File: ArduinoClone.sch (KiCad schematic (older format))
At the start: 13 parts, among them U1 DS1337S+, U2 24LC1025, U3 24LC1025, U4 ATMEGA328-AU, Y1 Crystal 32MHz, Y2 Crystal 16MHz

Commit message: added power flag
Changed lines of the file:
@@
 	7650 4850 7550 4850
 $Comp
-L power:GNDPWR #PWR?
+L power:GNDPWR #PWR0101
 U 1 1 5E9DFB73
 P 8750 5750
-F 0 "#PWR?" H 8750 5550 50  0001 C CNN
+F 0 "#PWR0101" H 8750 5550 50  0001 C CNN
 F 1 "GNDPWR" H 8754 5596 50  0000 C CNN
 F 2 "" H 8750 5700 50  0001 C CNN
@@
 	2900 1200 2900 1400
 $Comp
-L power:GNDPWR #PWR?
+L power:GNDPWR #PWR0102
 U 1 1 5E9F2D0F
 P 2900 2600
-F 0 "#PWR?" H 2900 2400 50  0001 C CNN
+F 0 "#PWR0102" H 2900 2400 50  0001 C CNN
 F 1 "GNDPWR" H 2904 2446 50  0000 C CNN
 F 2 "" H 2900 2550 50  0001 C CNN
@@
 	2600 3800 3450 3800
 $Comp
-L power:GNDPWR #PWR?
+L power:GNDPWR #PWR0103
 U 1 1 5E9FB7AB
 P 2800 4650
-F 0 "#PWR?" H 2800 4450 50  0001 C CNN
+F 0 "#PWR0103" H 2800 4450 50  0001 C CNN
 F 1 "GNDPWR" H 2804 4496 50  0000 C CNN
 F 2 "" H 2800 4600 50  0001 C CNN
@@
 ADDS2
 $Comp
-L power:GNDPWR #PWR?
+L power:GNDPWR #PWR0104
 U 1 1 5EA036F4
 P 9650 3200
-F 0 "#PWR?" H 9650 3000 50  0001 C CNN
+F 0 "#PWR0104" H 9650 3000 50  0001 C CNN
 F 1 "GNDPWR" H 9654 3046 50  0000 C CNN
 F 2 "" H 9650 3150 50  0001 C CNN
@@
 	9650 2000 9650 1700
 Wire Wire Line
-	9650 1700 7650 1700
+	9650 1700 8600 1700
 Connection ~ 7650 1700
 Wire Wire Line
@@
 	6350 2400 6200 2400
 $Comp
-L power:GNDPWR #PWR?
+L power:GNDPWR #PWR0105
 U 1 1 5EA0FFB6
 P 4750 2550
-F 0 "#PWR?" H 4750 2350 50  0001 C CNN
+F 0 "#PWR0105" H 4750 2350 50  0001 C CNN
 F 1 "GNDPWR" H 4754 2396 50  0000 C CNN
 F 2 "" H 4750 2500 50  0001 C CNN
@@
 	6150 3250 6950 3250
 $Comp
-L power:GNDPWR #PWR?
+L power:GNDPWR #PWR0106
 U 1 1 5EA19705
 P 5500 3900
-F 0 "#PWR?" H 5500 3700 50  0001 C CNN
+F 0 "#PWR0106" H 5500 3700 50  0001 C CNN
 F 1 "GNDPWR" H 5504 3746 50  0000 C CNN
 F 2 "" H 5500 3850 50  0001 C CNN
@@
 	6550 4700 6150 4700
 $Comp
-L power:GNDPWR #PWR?
+L power:GNDPWR #PWR0107
 U 1 1 5EA221DB
 P 7550 5300
-F 0 "#PWR?" H 7550 5100 50  0001 C CNN
+F 0 "#PWR0107" H 7550 5100 50  0001 C CNN
 F 1 "GNDPWR" H 7554 5146 50  0000 C CNN
 F 2 "" H 7550 5250 50  0001 C CNN
@@
 NoConn ~ 6950 4450
 NoConn ~ 6950 4550
+$Comp
+L power:PWR_FLAG #FLG0101
+U 1 1 5EA4EF3A
+P 8600 1700
+F 0 "#FLG0101" H 8600 1775 50  0001 C CNN
+F 1 "PWR_FLAG" H 8600 1873 50  0000 C CNN
+F 2 "" H 8600 1700 50  0001 C CNN
+F 3 "~" H 8600 1700 50  0001 C CNN
+	1    8600 1700
+	1    0    0    -1
+$EndComp
+Connection ~ 8600 1700
+Wire Wire Line
+	8600 1700 7650 1700
 $EndSCHEMATC

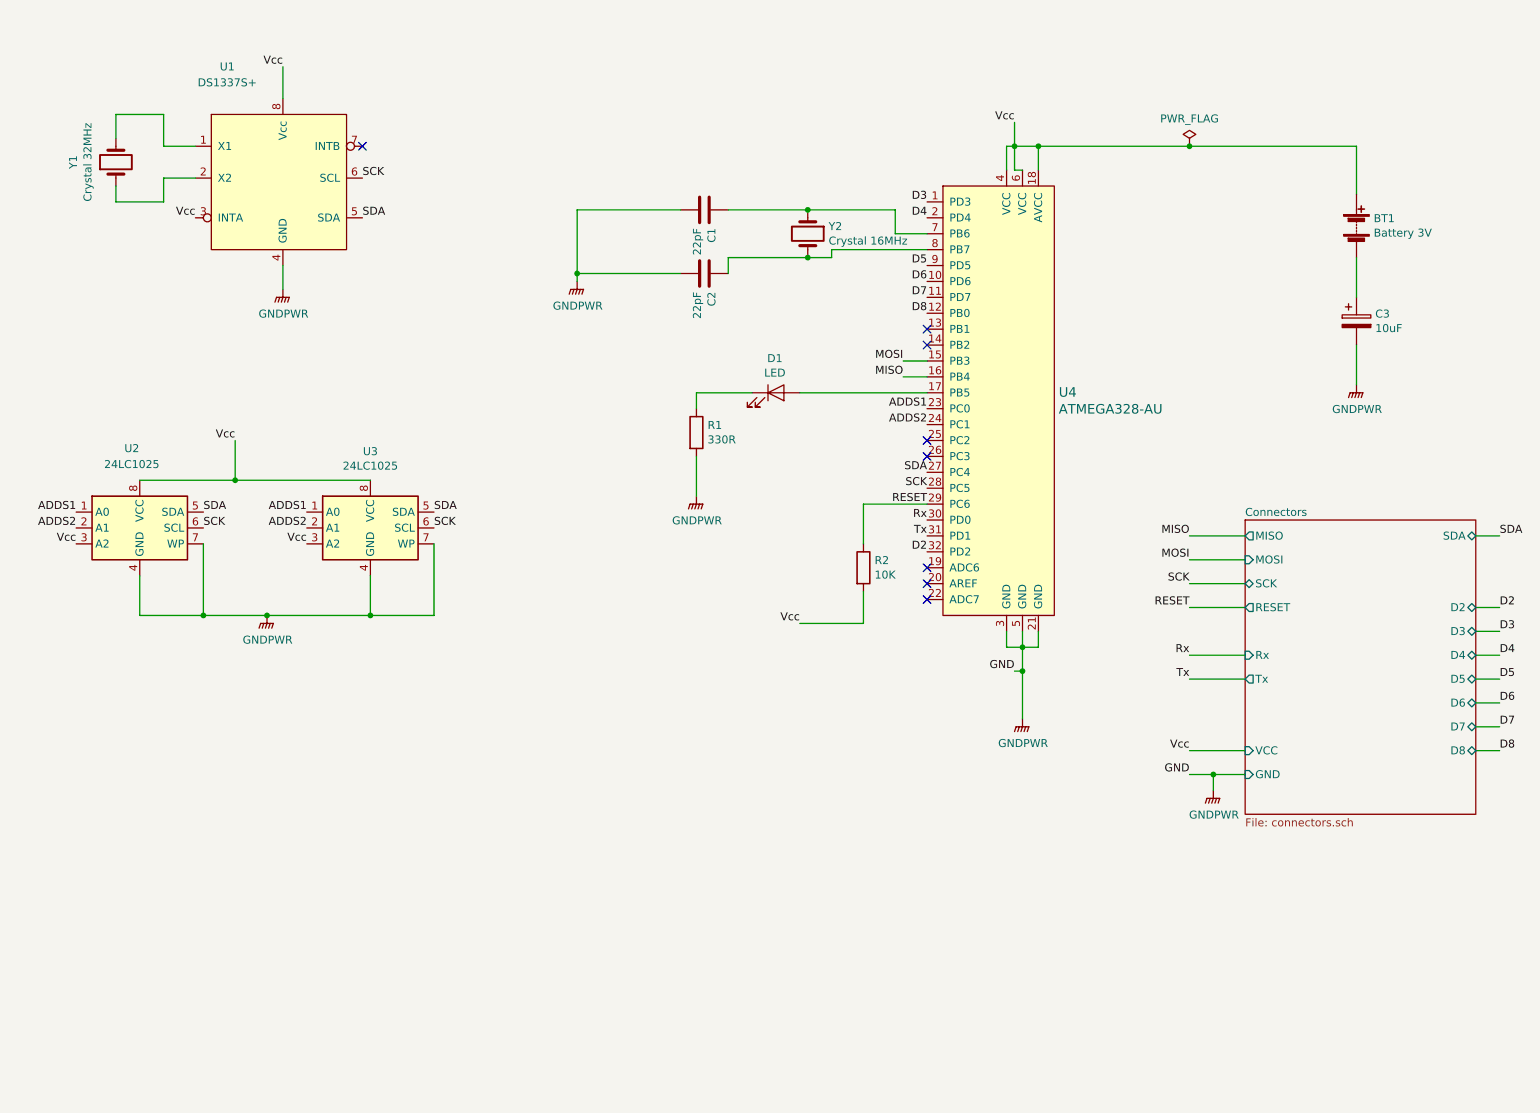
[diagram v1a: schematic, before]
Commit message: created netlist file
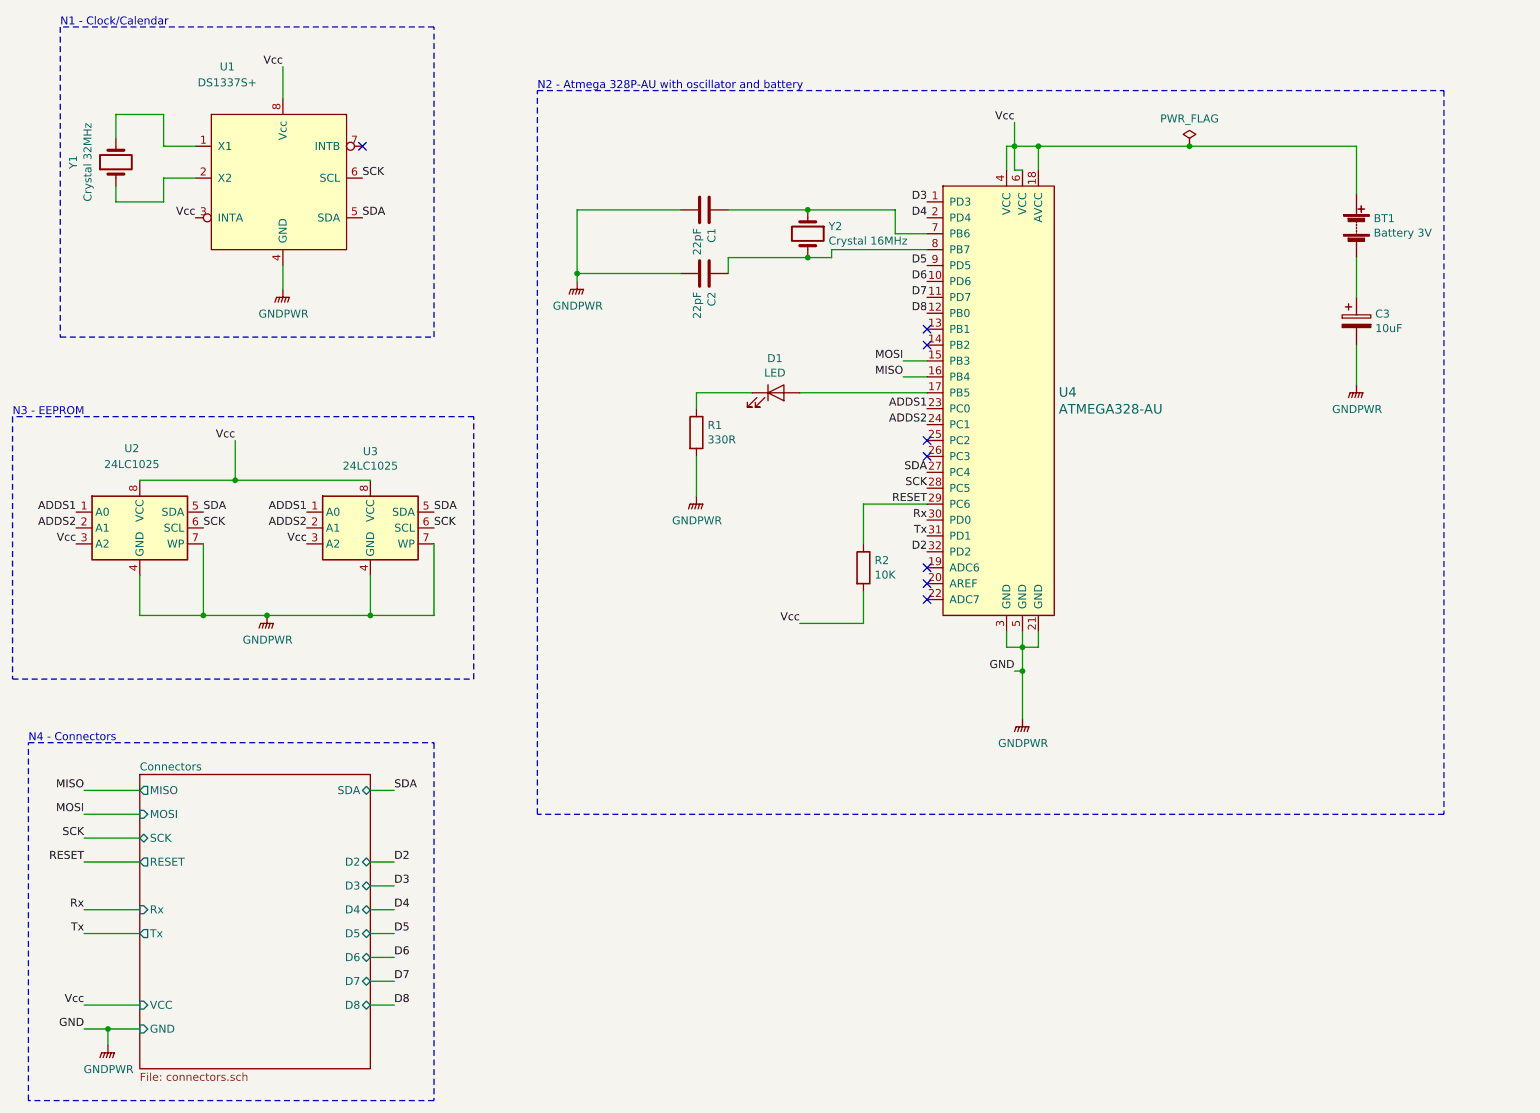
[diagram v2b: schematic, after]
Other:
- note added: "N1 - Clock/Calendar"
- note added: "N2 - Atmega 328P-AU with oscillator and battery"
- note added: "N3 - EEPROM"
- note added: "N4 - Connectors"
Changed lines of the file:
@@
 $EndComp
 $Sheet
-S 8950 4050 1450 1850
+S 2000 5650 1450 1850
 U 5E9B2945
 F0 "Connectors" 50
 F1 "connectors.sch" 50
-F2 "MISO" O L 8950 4150 50
-F3 "SCK" B L 8950 4450 50
-F4 "RESET" O L 8950 4600 50
-F5 "VCC" I L 8950 5500 50
-F6 "MOSI" I L 8950 4300 50
-F7 "GND" I L 8950 5650 50
-F8 "Rx" I L 8950 4900 50
-F9 "Tx" O L 8950 5050 50
-F10 "SDA" B R 10400 4150 50
-F11 "D2" B R 10400 4600 50
-F12 "D3" B R 10400 4750 50
-F13 "D4" B R 10400 4900 50
-F14 "D5" B R 10400 5050 50
-F15 "D6" B R 10400 5200 50
-F16 "D7" B R 10400 5350 50
-F17 "D8" B R 10400 5500 50
+F2 "MISO" O L 2000 5750 50
+F3 "SCK" B L 2000 6050 50
+F4 "RESET" O L 2000 6200 50
+F5 "VCC" I L 2000 7100 50
+F6 "MOSI" I L 2000 5900 50
+F7 "GND" I L 2000 7250 50
+F8 "Rx" I L 2000 6500 50
+F9 "Tx" O L 2000 6650 50
+F10 "SDA" B R 3450 5750 50
+F11 "D2" B R 3450 6200 50
+F12 "D3" B R 3450 6350 50
+F13 "D4" B R 3450 6500 50
+F14 "D5" B R 3450 6650 50
+F15 "D6" B R 3450 6800 50
+F16 "D7" B R 3450 6950 50
+F17 "D8" B R 3450 7100 50
 $EndSheet
 $Comp
@@
 	1    0    0    -1
 $EndComp
-Text Label 8600 4150 2    50   ~ 0
+Text Label 1650 5750 2    50   ~ 0
 MISO
 Wire Wire Line
-	8600 4150 8950 4150
+	1650 5750 2000 5750
 Text Label 6800 3150 2    50   ~ 0
 MISO
 Wire Wire Line
 	6800 3150 6950 3150
-Text Label 8600 4450 2    50   ~ 0
+Text Label 1650 6050 2    50   ~ 0
 SCK
 Wire Wire Line
-	8600 4450 8950 4450
-Text Label 8600 4600 2    50   ~ 0
+	1650 6050 2000 6050
+Text Label 1650 6200 2    50   ~ 0
 RESET
-Text Label 8600 5500 2    50   ~ 0
-Vcc
-Text Label 8600 4300 2    50   ~ 0
+Text Label 1650 7100 2    50   ~ 0
+Vcc
+Text Label 1650 5900 2    50   ~ 0
 MOSI
-Text Label 8600 5650 2    50   ~ 0
+Text Label 1650 7250 2    50   ~ 0
 GND
 Wire Wire Line
-	8600 4600 8950 4600
-Wire Wire Line
-	8600 5500 8950 5500
-Wire Wire Line
-	8600 4300 8950 4300
-Wire Wire Line
-	8600 5650 8750 5650
+	1650 6200 2000 6200
+Wire Wire Line
+	1650 7100 2000 7100
+Wire Wire Line
+	1650 5900 2000 5900
+Wire Wire Line
+	1650 7250 1800 7250
 Text Label 6800 3050 2    50   ~ 0
 MOSI
@@
 L power:GNDPWR #PWR0101
 U 1 1 5E9DFB73
-P 8750 5750
-F 0 "#PWR0101" H 8750 5550 50  0001 C CNN
-F 1 "GNDPWR" H 8754 5596 50  0000 C CNN
-F 2 "" H 8750 5700 50  0001 C CNN
-F 3 "" H 8750 5700 50  0001 C CNN
-	1    8750 5750
-	1    0    0    -1
-$EndComp
-Wire Wire Line
-	8750 5750 8750 5650
-Connection ~ 8750 5650
-Wire Wire Line
-	8750 5650 8950 5650
-Text Label 10550 4150 0    50   ~ 0
+P 1800 7350
+F 0 "#PWR0101" H 1800 7150 50  0001 C CNN
+F 1 "GNDPWR" H 1804 7196 50  0000 C CNN
+F 2 "" H 1800 7300 50  0001 C CNN
+F 3 "" H 1800 7300 50  0001 C CNN
+	1    1800 7350
+	1    0    0    -1
+$EndComp
+Wire Wire Line
+	1800 7350 1800 7250
+Connection ~ 1800 7250
+Wire Wire Line
+	1800 7250 2000 7250
+Text Label 3600 5750 0    50   ~ 0
 SDA
-Text Label 10550 4600 0    50   ~ 0
+Text Label 3600 6200 0    50   ~ 0
 D2
-Text Label 10550 4750 0    50   ~ 0
+Text Label 3600 6350 0    50   ~ 0
 D3
-Text Label 10550 4900 0    50   ~ 0
+Text Label 3600 6500 0    50   ~ 0
 D4
-Text Label 10550 5050 0    50   ~ 0
+Text Label 3600 6650 0    50   ~ 0
 D5
-Text Label 10550 5200 0    50   ~ 0
+Text Label 3600 6800 0    50   ~ 0
 D6
-Text Label 10550 5350 0    50   ~ 0
+Text Label 3600 6950 0    50   ~ 0
 D7
-Text Label 10550 5500 0    50   ~ 0
+Text Label 3600 7100 0    50   ~ 0
 D8
-Text Label 8600 5050 2    50   ~ 0
+Text Label 1650 6650 2    50   ~ 0
 Tx
-Text Label 8600 4900 2    50   ~ 0
+Text Label 1650 6500 2    50   ~ 0
 Rx
 Wire Wire Line
-	10550 4150 10400 4150
-Wire Wire Line
-	10550 4600 10400 4600
-Wire Wire Line
-	10550 4750 10400 4750
-Wire Wire Line
-	10550 4900 10400 4900
-Wire Wire Line
-	10550 5050 10400 5050
-Wire Wire Line
-	10550 5200 10400 5200
-Wire Wire Line
-	10550 5350 10400 5350
-Wire Wire Line
-	10550 5500 10400 5500
-Wire Wire Line
-	8600 4900 8950 4900
-Wire Wire Line
-	8600 5050 8950 5050
+	3600 5750 3450 5750
+Wire Wire Line
+	3600 6200 3450 6200
+Wire Wire Line
+	3600 6350 3450 6350
+Wire Wire Line
+	3600 6500 3450 6500
+Wire Wire Line
+	3600 6650 3450 6650
+Wire Wire Line
+	3600 6800 3450 6800
+Wire Wire Line
+	3600 6950 3450 6950
+Wire Wire Line
+	3600 7100 3450 7100
+Wire Wire Line
+	1650 6500 2000 6500
+Wire Wire Line
+	1650 6650 2000 6650
 Text Label 6950 2050 2    50   ~ 0
 D3
@@
 Wire Wire Line
 	8600 1700 7650 1700
+Wire Notes Line
+	3850 950  1500 950
+Wire Notes Line
+	1500 950  1500 2900
+Wire Notes Line
+	1500 2900 3850 2900
+Wire Notes Line
+	3850 2900 3850 950
+Wire Notes Line
+	4100 3400 1200 3400
+Wire Notes Line
+	1200 3400 1200 5050
+Wire Notes Line
+	1200 5050 4100 5050
+Wire Notes Line
+	4100 5050 4100 3400
+Wire Notes Line
+	4500 5900 4500 1350
+Wire Notes Line
+	4500 1350 10200 1350
+Wire Notes Line
+	10200 1350 10200 5900
+Wire Notes Line
+	10200 5900 4500 5900
+Text Notes 1500 950  0    50   ~ 0
+N1 - Clock/Calendar
+Text Notes 1200 3400 0    50   ~ 0
+N3 - EEPROM
+Text Notes 4500 1350 0    50   ~ 0
+N2 - Atmega 328P-AU with oscillator and battery
+Wire Notes Line
+	3850 5450 3850 7700
+Wire Notes Line
+	3850 7700 1300 7700
+Wire Notes Line
+	1300 7700 1300 5450
+Wire Notes Line
+	1300 5450 3850 5450
+Text Notes 1300 5450 0    50   ~ 0
+N4 - Connectors
 $EndSCHEMATC

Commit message: corrected error inschematic and placed components in pcbnew
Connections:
- net GNDPWR: now also BT1.2 (-)
- net Vcc: now also C3.1
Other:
- moved on the sheet: BT1
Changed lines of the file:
@@
 L Device:Battery BT1
 U 1 1 5E9ADC39
-P 9650 2200
-F 0 "BT1" H 9758 2246 50  0000 L CNN
-F 1 "Battery 3V" H 9758 2155 50  0000 L CNN
-F 2 "Connector_PinHeader_2.54mm:PinHeader_1x02_P2.54mm_Vertical" V 9650 2260 50  0001 C CNN
-F 3 "~" V 9650 2260 50  0001 C CNN
-	1    9650 2200
+P 9100 2800
+F 0 "BT1" H 9208 2846 50  0000 L CNN
+F 1 "Battery 3V" H 9208 2755 50  0000 L CNN
+F 2 "Connector_PinHeader_2.54mm:PinHeader_1x02_P2.54mm_Vertical" V 9100 2860 50  0001 C CNN
+F 3 "~" V 9100 2860 50  0001 C CNN
+	1    9100 2800
 	1    0    0    -1
 $EndComp
@@
 $EndComp
 Wire Wire Line
-	9650 2950 9650 3200
-Wire Wire Line
-	9650 2400 9650 2650
-Wire Wire Line
-	9650 2000 9650 1700
+	9650 2950 9650 3000
 Wire Wire Line
 	9650 1700 8600 1700
@@
 Text Notes 1300 5450 0    50   ~ 0
 N4 - Connectors
+Wire Wire Line
+	9650 1700 9650 2350
+Wire Wire Line
+	9650 2350 9100 2350
+Wire Wire Line
+	9100 2350 9100 2600
+Connection ~ 9650 2350
+Wire Wire Line
+	9650 2350 9650 2650
+Wire Wire Line
+	9100 3000 9650 3000
+Connection ~ 9650 3000
+Wire Wire Line
+	9650 3000 9650 3200
 $EndSCHEMATC
